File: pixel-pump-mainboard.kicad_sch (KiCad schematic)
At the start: 121 parts, among them J1 JST NC Valve, J10 BM10B-SRSS-TB(LF)(SN), J11 UART/SWD DNP, J12 TYPE-C-31-M-12, J2 JST NO Valve, J3 6P4C, J4 JST 3 Way Valve, J5 Jack-DC 12V, J6 Power Sw, J7 I2C, J8 SPI, J9 BM04B-SRSS-TBT(LF)(SN), Q1 BSS138, Q2 BSS138, Q3 BSS138, Q4 STN4NF20L, Q5 BSS138, SW1 BOOTSEL, U1 LD1117S33TR, U2 TPS62112RSAR, U3 W25Q128JVS, U4 RP2040, Y1 ABMM2-12.000MHZ-E2-T

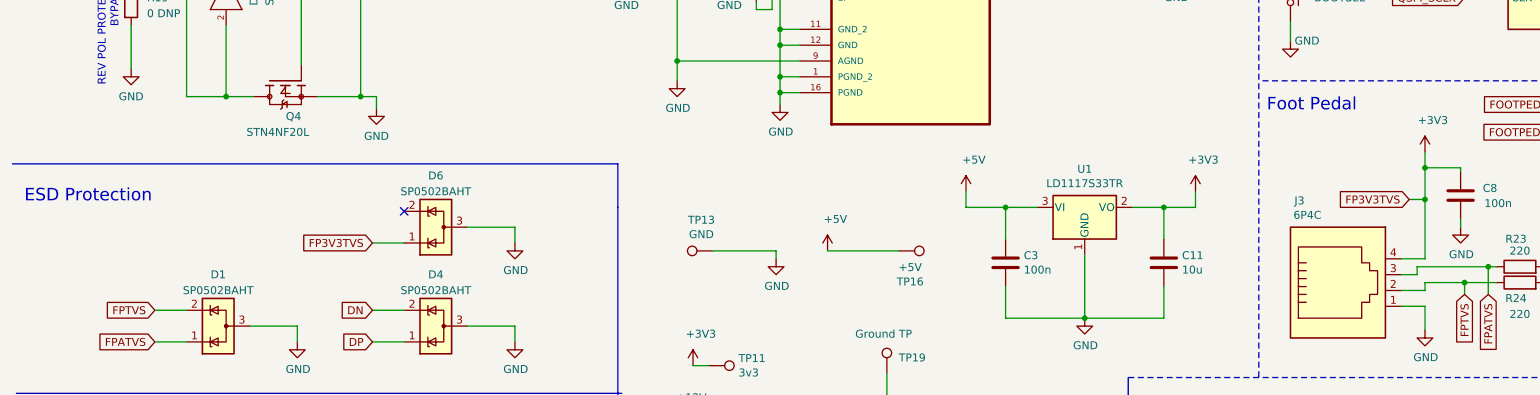
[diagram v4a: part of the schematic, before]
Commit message: Updated layout for EMI specific changes
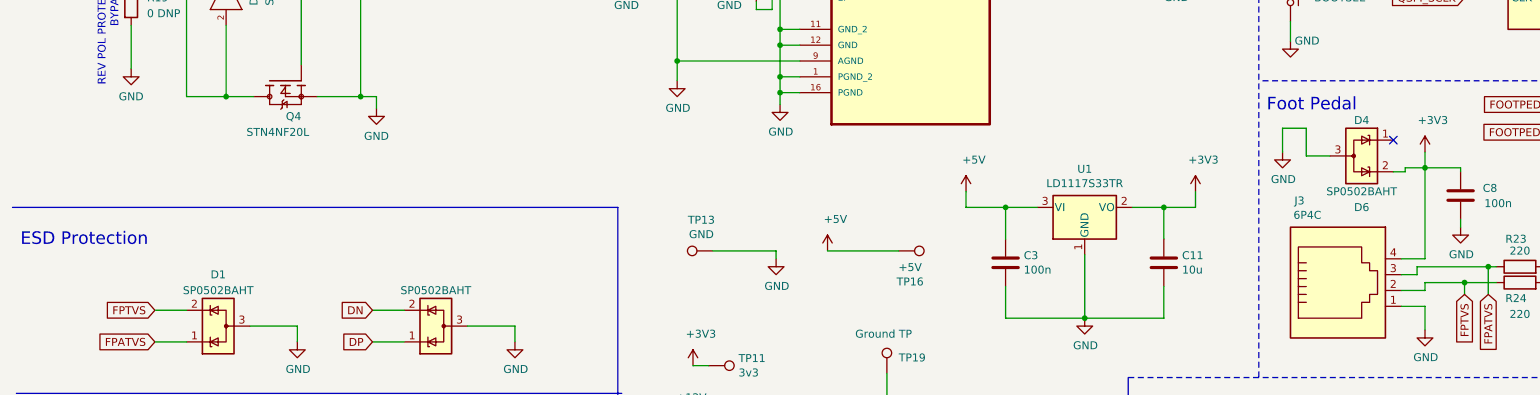
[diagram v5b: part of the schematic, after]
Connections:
- net +3V3: now also D6.2 (K); no longer D6.1 (K)
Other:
- moved on the sheet: D6
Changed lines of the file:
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@@
   (junction (at 46.99 67.945) (diameter 0.9144) (color 0 0 0 0)
   )
-  (junction (at 239.395 175.895) (diameter 0) (color 0 0 0 0)
-  )
   (junction (at 346.075 46.355) (diameter 0.9144) (color 0 0 0 0)
   )
@@
   (no_connect (at 374.015 144.78))
   (no_connect (at 74.93 225.425))
-  (no_connect (at 75.565 177.8))
+  (no_connect (at 234.315 166.37))
   (wire (pts (xy 201.93 248.285) (xy 212.09 248.285))
     (stroke (width 0) (type solid) (color 0 0 0 0))
@@
     (stroke (width 0) (type solid) (color 0 0 0 0))
   )
-  (wire (pts (xy 93.345 180.34) (xy 93.345 182.88))
-    (stroke (width 0) (type solid) (color 0 0 0 0))
-  )
   (polyline (pts (xy 109.855 207.01) (xy 109.855 284.48))
     (stroke (width 0) (type default) (color 0 0 0 0))
@@
     (stroke (width 0) (type solid) (color 0 0 0 0))
   )
-  (polyline (pts (xy 12.7 170.18) (xy 109.855 170.18))
+  (polyline (pts (xy 12.7 177.165) (xy 109.855 177.165))
     (stroke (width 0) (type default) (color 0 0 0 0))
   )
@@
     (stroke (width 0) (type solid) (color 0 0 0 0))
   )
+  (wire (pts (xy 220.345 168.91) (xy 220.345 164.465))
+    (stroke (width 0) (type default) (color 0 0 0 0))
+  )
   (wire (pts (xy 403.225 214.63) (xy 402.59 214.63))
     (stroke (width 0) (type solid) (color 0 0 0 0))
@@
     (stroke (width 0) (type solid) (color 0 0 0 0))
   )
+  (wire (pts (xy 236.22 170.815) (xy 239.395 170.815))
+    (stroke (width 0) (type default) (color 0 0 0 0))
+  )
   (wire (pts (xy 258.445 186.69) (xy 260.985 186.69))
     (stroke (width 0) (type solid) (color 0 0 0 0))
@@
     (stroke (width 0) (type solid) (color 0 0 0 0))
   )
+  (wire (pts (xy 224.155 168.91) (xy 220.345 168.91))
+    (stroke (width 0) (type default) (color 0 0 0 0))
+  )
   (wire (pts (xy 176.53 62.23) (xy 181.61 62.23))
     (stroke (width 0) (type solid) (color 0 0 0 0))
@@
     (stroke (width 0) (type solid) (color 0 0 0 0))
   )
-  (wire (pts (xy 236.855 175.895) (xy 239.395 175.895))
-    (stroke (width 0) (type default) (color 0 0 0 0))
-  )
   (wire (pts (xy 184.785 194.945) (xy 184.785 184.785))
     (stroke (width 0) (type solid) (color 0 0 0 0))
@@
     (stroke (width 0) (type dash) (color 0 0 0 0))
   )
+  (wire (pts (xy 236.22 171.45) (xy 236.22 170.815))
+    (stroke (width 0) (type default) (color 0 0 0 0))
+  )
   (wire (pts (xy 50.8 196.215) (xy 58.42 196.215))
     (stroke (width 0) (type solid) (color 0 0 0 0))
@@
     (stroke (width 0) (type solid) (color 0 0 0 0))
   )
+  (wire (pts (xy 216.535 164.465) (xy 216.535 168.275))
+    (stroke (width 0) (type default) (color 0 0 0 0))
+  )
   (wire (pts (xy 249.555 186.69) (xy 250.825 186.69))
     (stroke (width 0) (type solid) (color 0 0 0 0))
@@
     (stroke (width 0) (type solid) (color 0 0 0 0))
   )
-  (wire (pts (xy 239.395 170.815) (xy 239.395 175.895))
-    (stroke (width 0) (type default) (color 0 0 0 0))
-  )
   (wire (pts (xy 119.38 123.19) (xy 119.38 128.27))
     (stroke (width 0) (type solid) (color 0 0 0 0))
@@
     (stroke (width 0) (type solid) (color 0 0 0 0))
   )
+  (wire (pts (xy 234.315 171.45) (xy 236.22 171.45))
+    (stroke (width 0) (type default) (color 0 0 0 0))
+  )
   (wire (pts (xy 245.745 143.51) (xy 250.19 143.51))
     (stroke (width 0) (type solid) (color 0 0 0 0))
@@
     (stroke (width 0) (type default) (color 0 0 0 0))
   )
-  (wire (pts (xy 85.725 180.34) (xy 93.345 180.34))
-    (stroke (width 0) (type solid) (color 0 0 0 0))
-  )
   (wire (pts (xy 307.34 133.35) (xy 310.515 133.35))
     (stroke (width 0) (type solid) (color 0 0 0 0))
@@
     (stroke (width 0) (type solid) (color 0 0 0 0))
   )
+  (wire (pts (xy 220.345 164.465) (xy 216.535 164.465))
+    (stroke (width 0) (type default) (color 0 0 0 0))
+  )
   (wire (pts (xy 81.28 243.205) (xy 81.28 245.745))
     (stroke (width 0) (type solid) (color 0 0 0 0))
@@
     (stroke (width 0) (type solid) (color 0 0 0 0))
   )
-  (polyline (pts (xy 109.855 177.165) (xy 109.855 170.18))
-    (stroke (width 0) (type default) (color 0 0 0 0))
-  )
   (wire (pts (xy 338.455 32.385) (xy 338.455 46.355))
     (stroke (width 0) (type solid) (color 0 0 0 0))
@@
     (stroke (width 0) (type solid) (color 0 0 0 0))
   )
-  (wire (pts (xy 325.755 36.83) (xy 325.755 38.1))
+  (wire (pts (xy 239.395 170.815) (xy 239.395 185.42))
     (stroke (width 0) (type default) (color 0 0 0 0))
   )
-  (wire (pts (xy 239.395 175.895) (xy 239.395 185.42))
+  (wire (pts (xy 325.755 36.83) (xy 325.755 38.1))
     (stroke (width 0) (type default) (color 0 0 0 0))
   )
@@
     (stroke (width 0) (type solid) (color 0 0 0 0))
   )
-  (wire (pts (xy 70.485 182.88) (xy 75.565 182.88))
-    (stroke (width 0) (type default) (color 0 0 0 0))
-  )
   (wire (pts (xy 374.015 88.9) (xy 379.095 88.9))
     (stroke (width 0) (type solid) (color 0 0 0 0))
@@
     (stroke (width 0) (type solid) (color 0 0 0 0))
   )
-  (text "ESD Protection" (at 14.605 176.53 0)
+  (text "ESD Protection" (at 13.97 183.515 0)
     (effects (font (size 2.0066 2.0066)) (justify left bottom))
   )
@@
     )
   )
-  (global_label "FP3V3TVS" (shape input) (at 70.485 182.88 180) (fields_autoplaced)
-    (effects (font (size 1.27 1.27)) (justify right))
-    (property "Intersheet References" "${INTERSHEET_REFS}" (id 0) (at 58.7495 182.8006 0)
-      (effects (font (size 1.27 1.27)) (justify right) hide)
-    )
-  )
   (global_label "QSPI_SD2" (shape input) (at 279.4 143.51 0)
     (effects (font (size 1.27 1.27)) (justify left))
@@
     )
   )
-  (global_label "FP3V3TVS" (shape input) (at 236.855 175.895 180) (fields_autoplaced)
-    (effects (font (size 1.27 1.27)) (justify right))
-    (property "Intersheet References" "${INTERSHEET_REFS}" (id 0) (at 225.1195 175.8156 0)
-      (effects (font (size 1.27 1.27)) (justify right) hide)
-    )
-  )
   (global_label "QSPI_SD3" (shape input) (at 307.34 81.28 180)
     (effects (font (size 1.27 1.27)) (justify right))
@@
     (pin "2")
   )
-  (symbol (lib_id "power:GND") (at 93.345 182.88 0) (unit 1)
+  (symbol (lib_id "power:GND") (at 216.535 168.275 0) (unit 1)
     (in_bom yes) (on_board yes)
-    (property "Reference" "#PWR047" (id 0) (at 93.345 189.23 0)
+    (property "Reference" "#PWR047" (id 0) (at 216.535 174.625 0)
       (effects (font (size 1.27 1.27)) hide)
     )
-    (property "Value" "GND" (id 1) (at 93.472 187.2742 0))
-    (property "Footprint" "" (id 2) (at 93.345 182.88 0)
+    (property "Value" "GND" (id 1) (at 216.662 172.6692 0))
+    (property "Footprint" "" (id 2) (at 216.535 168.275 0)
       (effects (font (size 1.27 1.27)) hide)
     )
-    (property "Datasheet" "" (id 3) (at 93.345 182.88 0)
+    (property "Datasheet" "" (id 3) (at 216.535 168.275 0)
       (effects (font (size 1.27 1.27)) hide)
     )
     (pin "1")
   )
-  (symbol (lib_id "Power_Protection:SP0502BAHT") (at 80.645 180.34 90) (unit 1)
+  (symbol (lib_id "Power_Protection:SP0502BAHT") (at 229.235 168.91 270) (unit 1)
     (in_bom yes) (on_board yes) (fields_autoplaced)
-    (property "Reference" "D6" (id 0) (at 80.645 172.085 90))
-    (property "Value" "SP0502BAHT" (id 1) (at 80.645 174.625 90))
-    (property "Footprint" "Package_TO_SOT_SMD:SOT-23" (id 2) (at 81.915 174.625 0)
+    (property "Reference" "D6" (id 0) (at 229.235 177.165 90))
+    (property "Value" "SP0502BAHT" (id 1) (at 229.235 174.625 90))
+    (property "Footprint" "Package_TO_SOT_SMD:SOT-23" (id 2) (at 227.965 174.625 0)
       (effects (font (size 1.27 1.27)) (justify left) hide)
     )
-    (property "Datasheet" "http://www.littelfuse.com/~/media/files/littelfuse/technical%20resources/documents/data%20sheets/sp05xxba.pdf" (id 3) (at 77.47 177.165 0)
+    (property "Datasheet" "http://www.littelfuse.com/~/media/files/littelfuse/technical%20resources/documents/data%20sheets/sp05xxba.pdf" (id 3) (at 232.41 172.085 0)
       (effects (font (size 1.27 1.27)) hide)
     )
@@
   (symbol (lib_id "Power_Protection:SP0502BAHT") (at 80.645 196.215 90) (unit 1)
     (in_bom yes) (on_board yes)
-    (property "Reference" "D4" (id 0) (at 80.645 187.96 90))
+    (property "Reference" "D4" (id 0) (at 229.235 163.195 90))
     (property "Value" "SP0502BAHT" (id 1) (at 80.645 190.5 90))
     (property "Footprint" "Package_TO_SOT_SMD:SOT-23" (id 2) (at 81.915 190.5 0)

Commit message: Finish EMI changes
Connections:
- net at C5.1, F1.1, J6.1 (Pin_1)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: no longer D5.1
- net at F1.2, J5.1: now also D5.1
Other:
- moved on the sheet: F1
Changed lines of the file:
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@@
   (junction (at 132.08 245.11) (diameter 1.016) (color 0 0 0 0)
   )
+  (junction (at 46.99 129.54) (diameter 0) (color 0 0 0 0)
+  )
   (junction (at 389.255 40.005) (diameter 0.9144) (color 0 0 0 0)
   )
@@
   (junction (at 353.695 40.005) (diameter 0.9144) (color 0 0 0 0)
   )
+  (junction (at 59.055 129.54) (diameter 0) (color 0 0 0 0)
+  )
   (junction (at 274.32 234.95) (diameter 0.9144) (color 0 0 0 0)
   )
@@
   (junction (at 340.995 46.355) (diameter 0.9144) (color 0 0 0 0)
   )
-  (junction (at 46.99 129.54) (diameter 0) (color 0 0 0 0)
-  )
   (junction (at 354.965 46.355) (diameter 0.9144) (color 0 0 0 0)
   )
@@
   (junction (at 58.42 37.465) (diameter 0.9144) (color 0 0 0 0)
   )
-  (junction (at 59.055 129.54) (diameter 0) (color 0 0 0 0)
-  )
   (junction (at 81.28 255.905) (diameter 0.9144) (color 0 0 0 0)
   )
@@
     (stroke (width 0) (type solid) (color 0 0 0 0))
   )
+  (wire (pts (xy 46.99 129.54) (xy 29.21 129.54))
+    (stroke (width 0) (type default) (color 0 0 0 0))
+  )
   (wire (pts (xy 235.585 185.42) (xy 239.395 185.42))
     (stroke (width 0) (type solid) (color 0 0 0 0))
@@
     (stroke (width 0) (type solid) (color 0 0 0 0))
   )
+  (wire (pts (xy 46.99 132.715) (xy 46.99 129.54))
+    (stroke (width 0) (type default) (color 0 0 0 0))
+  )
   (wire (pts (xy 208.915 219.075) (xy 212.725 219.075))
     (stroke (width 0) (type solid) (color 0 0 0 0))
@@
     (stroke (width 0) (type solid) (color 0 0 0 0))
   )
-  (wire (pts (xy 40.005 129.54) (xy 46.99 129.54))
-    (stroke (width 0) (type default) (color 0 0 0 0))
-  )
   (wire (pts (xy 333.375 233.68) (xy 339.09 233.68))
     (stroke (width 0) (type solid) (color 0 0 0 0))
@@
     (stroke (width 0) (type solid) (color 0 0 0 0))
   )
-  (wire (pts (xy 46.99 129.54) (xy 59.055 129.54))
-    (stroke (width 0) (type default) (color 0 0 0 0))
-  )
   (wire (pts (xy 68.58 159.385) (xy 71.12 159.385))
     (stroke (width 0) (type solid) (color 0 0 0 0))
@@
     (stroke (width 0) (type solid) (color 0 0 0 0))
   )
-  (wire (pts (xy 29.21 129.54) (xy 32.385 129.54))
-    (stroke (width 0) (type default) (color 0 0 0 0))
-  )
   (wire (pts (xy 132.08 144.145) (xy 132.08 145.415))
     (stroke (width 0) (type solid) (color 0 0 0 0))
@@
     (stroke (width 0) (type solid) (color 0 0 0 0))
   )
-  (wire (pts (xy 46.99 129.54) (xy 46.99 132.715))
-    (stroke (width 0) (type default) (color 0 0 0 0))
-  )
   (wire (pts (xy 307.34 133.35) (xy 310.515 133.35))
     (stroke (width 0) (type solid) (color 0 0 0 0))
@@
     (stroke (width 0) (type solid) (color 0 0 0 0))
   )
+  (wire (pts (xy 46.99 129.54) (xy 49.53 129.54))
+    (stroke (width 0) (type default) (color 0 0 0 0))
+  )
   (wire (pts (xy 46.99 67.945) (xy 50.8 67.945))
     (stroke (width 0) (type solid) (color 0 0 0 0))
@@
     (stroke (width 0) (type solid) (color 0 0 0 0))
   )
+  (wire (pts (xy 57.15 129.54) (xy 59.055 129.54))
+    (stroke (width 0) (type default) (color 0 0 0 0))
+  )
   (wire (pts (xy 274.955 125.095) (xy 274.955 127))
     (stroke (width 0) (type solid) (color 0 0 0 0))
@@
     (pin "1")
   )
-  (symbol (lib_id "Device:Polyfuse") (at 36.195 129.54 270) (unit 1)
+  (symbol (lib_id "Device:Polyfuse") (at 53.34 129.54 270) (unit 1)
     (in_bom yes) (on_board yes)
-    (property "Reference" "F1" (id 0) (at 36.195 123.1138 90))
-    (property "Value" "1812L075PR" (id 1) (at 36.195 125.6538 90))
-    (property "Footprint" "Fuse:Fuse_1812_4532Metric" (id 2) (at 31.115 130.81 0)
+    (property "Reference" "F1" (id 0) (at 53.34 123.1138 90))
+    (property "Value" "1812L075PR" (id 1) (at 53.34 125.6538 90))
+    (property "Footprint" "Fuse:Fuse_1812_4532Metric" (id 2) (at 48.26 130.81 0)
       (effects (font (size 1.27 1.27)) (justify left) hide)
     )
-    (property "Datasheet" "~" (id 3) (at 36.195 129.54 0)
+    (property "Datasheet" "~" (id 3) (at 53.34 129.54 0)
       (effects (font (size 1.27 1.27)) hide)
     )
-    (property "Source" "https://lcsc.com/product-detail/PTC-Resettable-Fuses_Littelfuse-1812L075PR_C142689.html" (id 4) (at 36.195 129.54 0)
+    (property "Source" "https://lcsc.com/product-detail/PTC-Resettable-Fuses_Littelfuse-1812L075PR_C142689.html" (id 4) (at 53.34 129.54 0)
       (effects (font (size 1.27 1.27)) hide)
     )

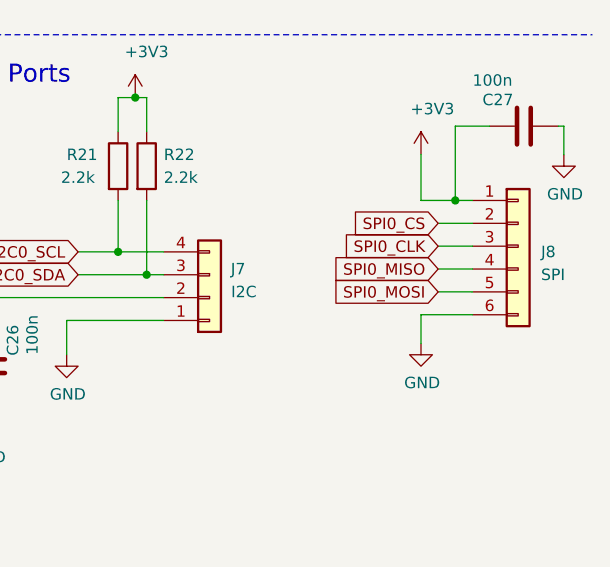
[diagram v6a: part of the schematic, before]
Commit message: Rename ports to EXP1 and EXP2 and reduce mousebite stiffness
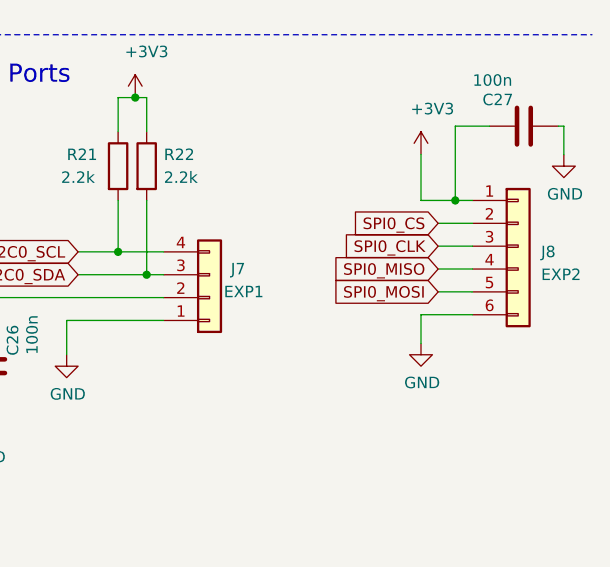
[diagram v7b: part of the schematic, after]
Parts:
- J7: value I2C -> EXP1
- J8: value SPI -> EXP2
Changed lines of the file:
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@@
     (title "Pixel Pump Mainboard")
     (date "2020-12-18")
-    (rev "3")
-    (comment 1 "Revision Date 2022-01-11")
+    (rev "4")
+    (comment 1 "Revision Date 2022-04-29")
   )
   (junction (at 135.89 148.59) (diameter 0.9144) (color 0 0 0 0)
@@
     (in_bom yes) (on_board yes)
     (property "Reference" "J7" (id 0) (at 367.03 230.505 0))
-    (property "Value" "I2C" (id 1) (at 367.665 233.045 0))
+    (property "Value" "EXP1" (id 1) (at 367.665 233.045 0))
     (property "Footprint" "Connector_JST:JST_SH_BM04B-SRSS-TB_1x04-1MP_P1.00mm_Vertical" (id 2) (at 363.855 233.68 0)
       (effects (font (size 1.27 1.27)) hide)
@@
       (effects (font (size 1.27 1.27)) (justify left))
     )
-    (property "Value" "SPI" (id 1) (at 400.685 231.14 0)
+    (property "Value" "EXP2" (id 1) (at 400.685 231.14 0)
       (effects (font (size 1.27 1.27)) (justify left))
     )
@@
     )
     (path "/63c15b5e-c12a-4523-afda-c3d21e50ba5b"
-      (reference "J7") (unit 1) (value "I2C") (footprint "Connector_JST:JST_SH_BM04B-SRSS-TB_1x04-1MP_P1.00mm_Vertical")
+      (reference "J7") (unit 1) (value "EXP1") (footprint "Connector_JST:JST_SH_BM04B-SRSS-TB_1x04-1MP_P1.00mm_Vertical")
     )
     (path "/ccde1372-9ab3-47ad-9572-4de6238d460d"
-      (reference "J8") (unit 1) (value "SPI") (footprint "Connector_JST:JST_SH_BM06B-SRSS-TB_1x06-1MP_P1.00mm_Vertical")
+      (reference "J8") (unit 1) (value "EXP2") (footprint "Connector_JST:JST_SH_BM06B-SRSS-TB_1x06-1MP_P1.00mm_Vertical")
     )
     (path "/e5c2696e-219e-4607-9e22-8a199dce175a"
